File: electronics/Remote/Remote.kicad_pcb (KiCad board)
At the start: 2 copper layers, 111.8 x 38.1 mm, 25 parts, among them J2 Conn_01x10_Pin, SW1 SW_SPST, SW2 SW_SPST, SW3 SW_SPST, SW4 SW_SPST, SW5 SW_SPST

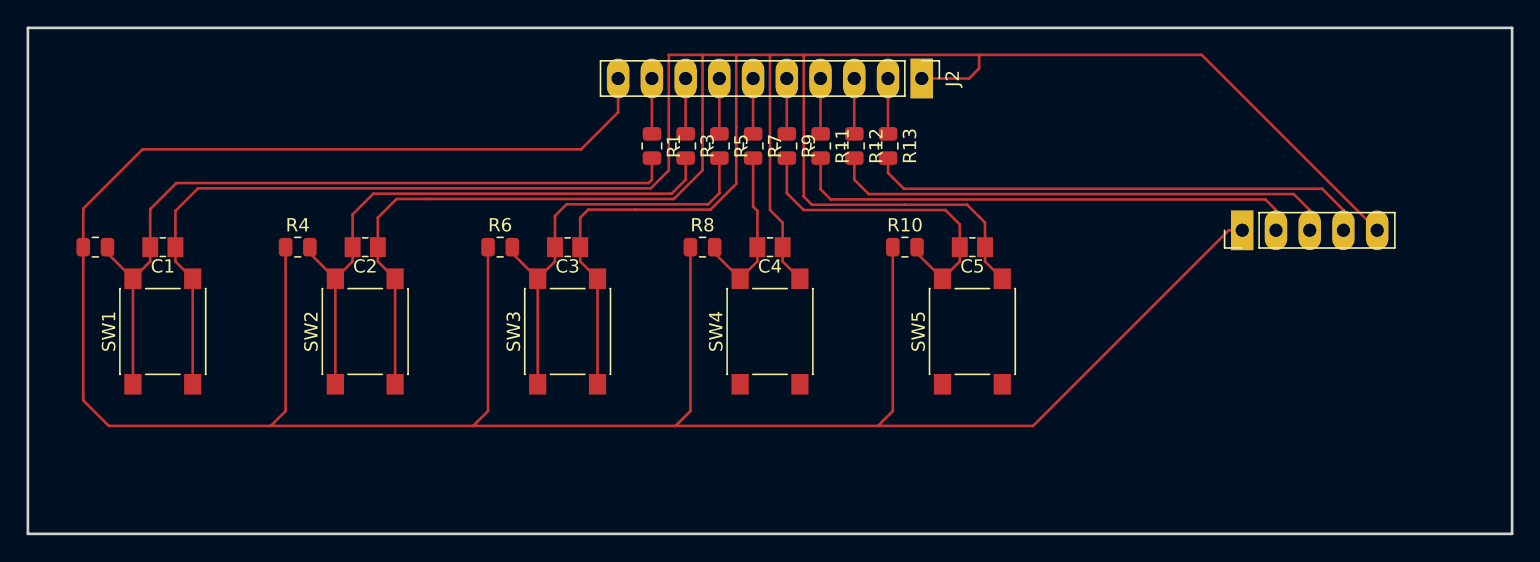
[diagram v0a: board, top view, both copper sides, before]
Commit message: Basic remote button interface created.
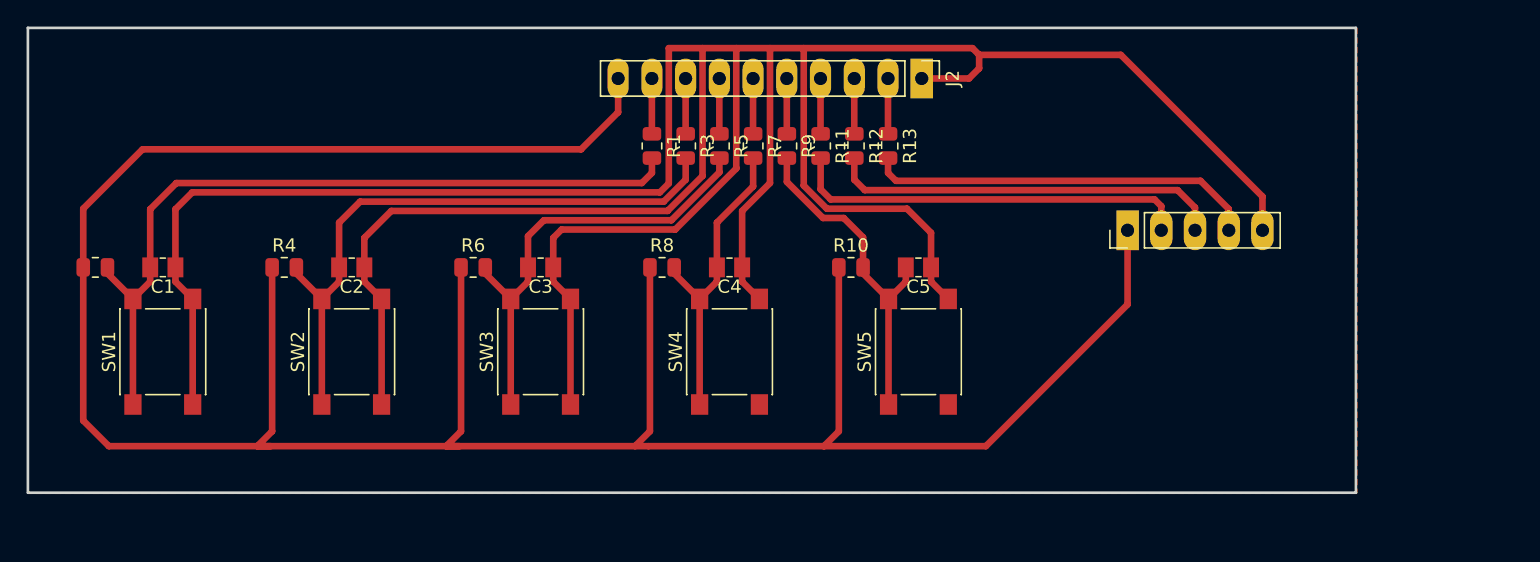
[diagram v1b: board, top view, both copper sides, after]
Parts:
- moved J1 8.64 mm to (159.0, 76.2)
- moved R10 4.34 mm to (138.2, 79.0)
- moved C5 4.34 mm to (143.3, 79.0)
- moved SW5 4.34 mm to (143.3, 85.3)
- moved C4 3.41 mm to (129.0, 79.0)
- moved R8 3.41 mm to (124.0, 79.0)
- moved SW4 3.41 mm to (129.0, 85.3)
- moved R6 2.54 mm to (109.7, 79.0)
- moved C3 2.54 mm to (114.8, 79.0)
- moved SW3 2.54 mm to (114.8, 85.3)
- moved C2 1.83 mm to (100.6, 79.0)
- moved R4 1.83 mm to (95.5, 79.0)
- moved SW2 1.83 mm to (100.6, 85.3)
- moved C1 1.52 mm to (86.4, 79.0)
- moved R2 1.52 mm to (81.3, 79.0)
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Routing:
- net Net-(SW4-A): track 12.9 -> 23.4 mm
- net Net-(J1-S1): track 38.1 -> 29.5 mm
- net Net-(J1-S2): track 38.4 -> 29.9 mm
- net Net-(J1-Button): track 38.8 -> 30.3 mm
- net Net-(SW2-A): track 44.3 -> 46.5 mm
- net Net-(SW3-A): track 32.1 -> 33.9 mm
- net Net-(SW1-A): track 57.2 -> 58.4 mm
- net 3V3: track 210.1 -> 209.0 mm
- net Net-(SW5-A): track 24.4 -> 25.6 mm
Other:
- board size 111.8 x 38.1 mm -> 100 x 35 mm
